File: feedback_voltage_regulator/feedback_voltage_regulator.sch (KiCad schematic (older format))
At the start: 25 parts, among them J1 Power input, J10 Ground point 1, J11 Ground point 2, J12 Input current probe, J13 Ground point 3, J14 Ground point 5, J18 Input current probe, J19 Input current probe, J2 Input current probe, J20 Current short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

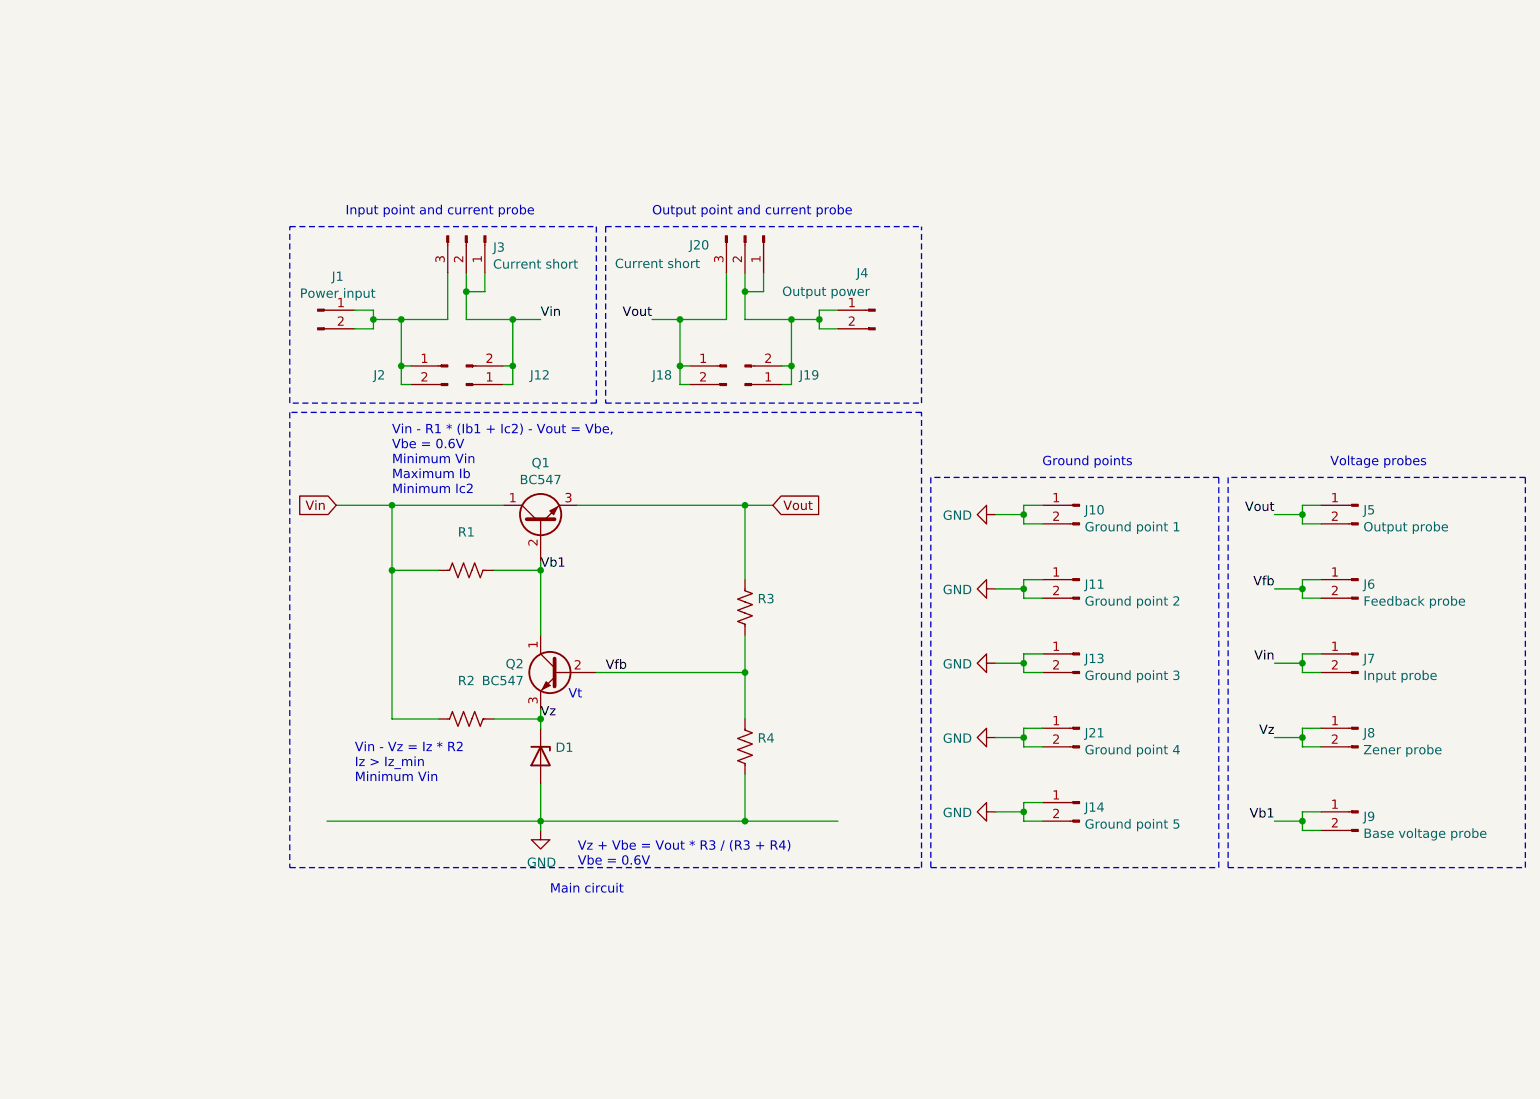
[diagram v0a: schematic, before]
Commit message: Updated schematic symbols and size
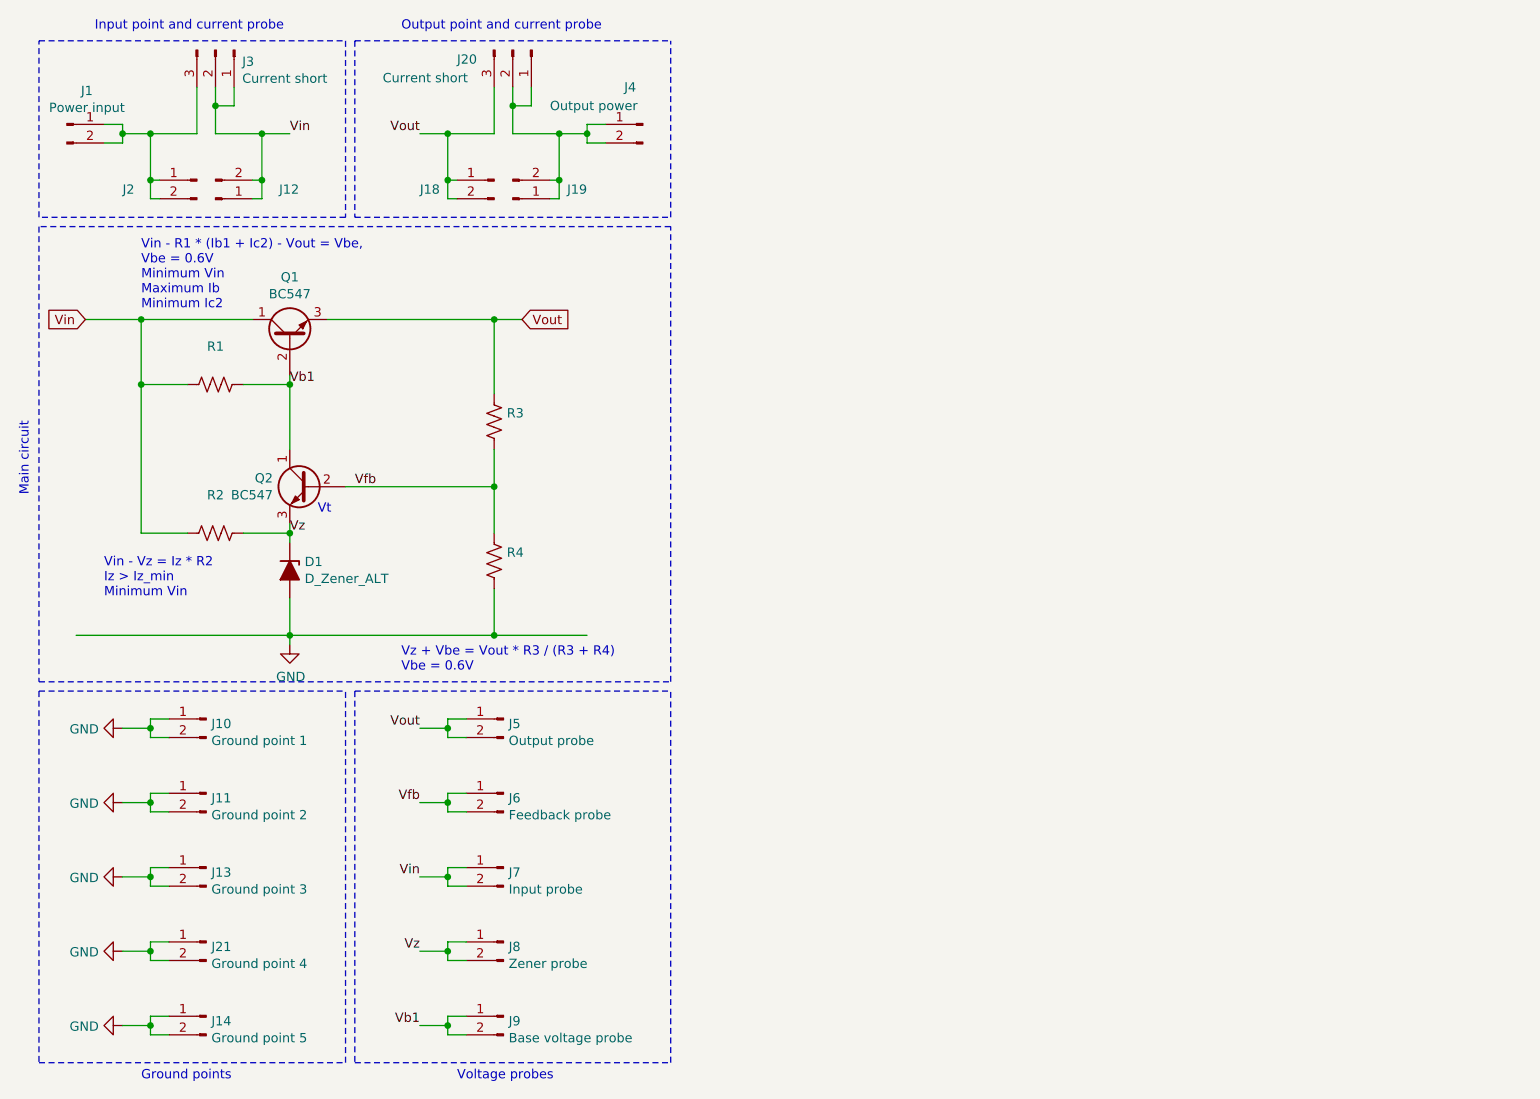
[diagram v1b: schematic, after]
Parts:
- removed D1: D_Zener, Diode_THT:D_DO-15_P15.24mm_Horizontal, symbol Device:D_Zener
- added D1: D_Zener_ALT, Diode_THT:D_DO-15_P15.24mm_Horizontal, symbol Device:D_Zener_ALT
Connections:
- net GND: now also D1.2 (A)
- net Vz: now also D1.1 (K)
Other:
- moved on the sheet: J1, J10, J11, J12, J13, J14, J18, J19, J2, J20, J21, J3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
